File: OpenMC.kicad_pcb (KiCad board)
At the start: 2 copper layers, 38.1 x 38.1 mm, 142 parts, among them J1 Motor Digital, J2 USB-C, J3 CAN, J4 Controller, J5 Motor Analog, SW1 RESET, SW2 BOOT, SW5 POS, U1 ESP32-S3, U3 TCAN332G, U5 NCP163ASN330T1G, Y1 40MHz

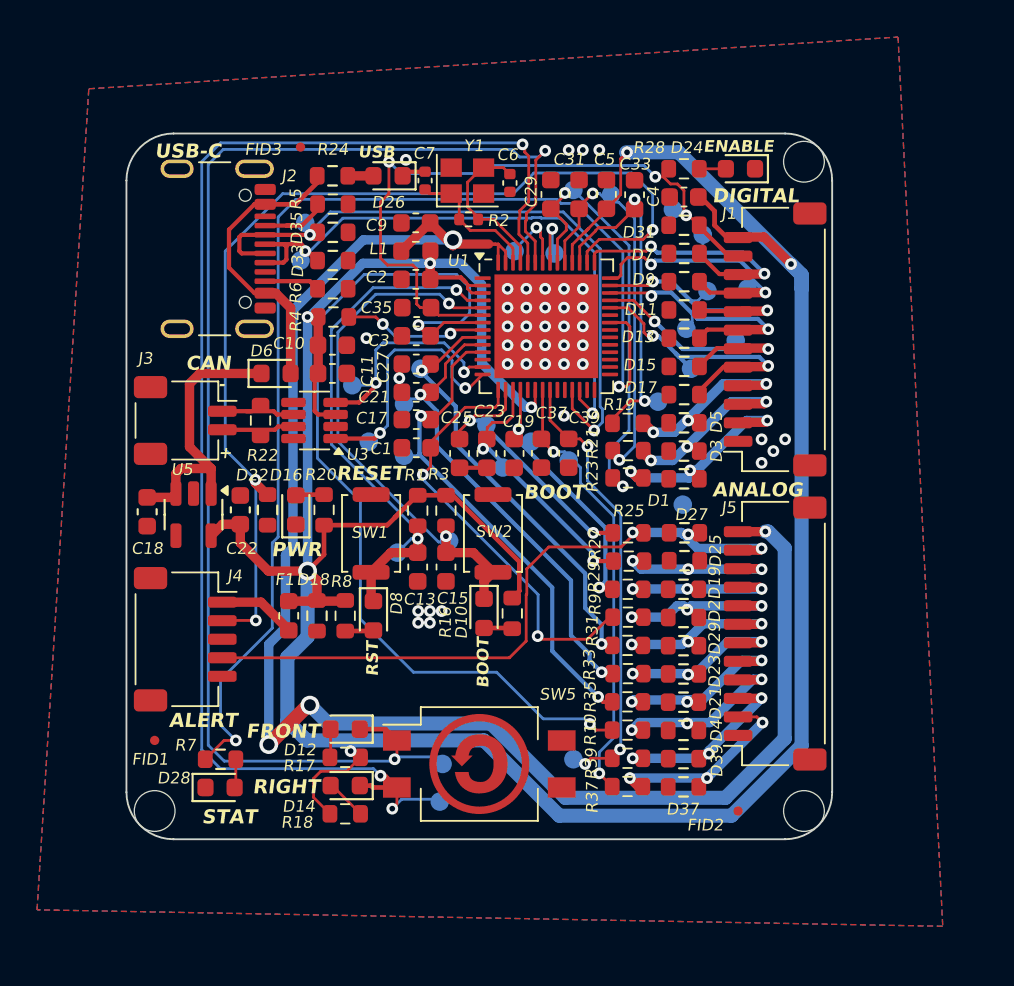
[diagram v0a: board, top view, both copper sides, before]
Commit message: updated to external adc
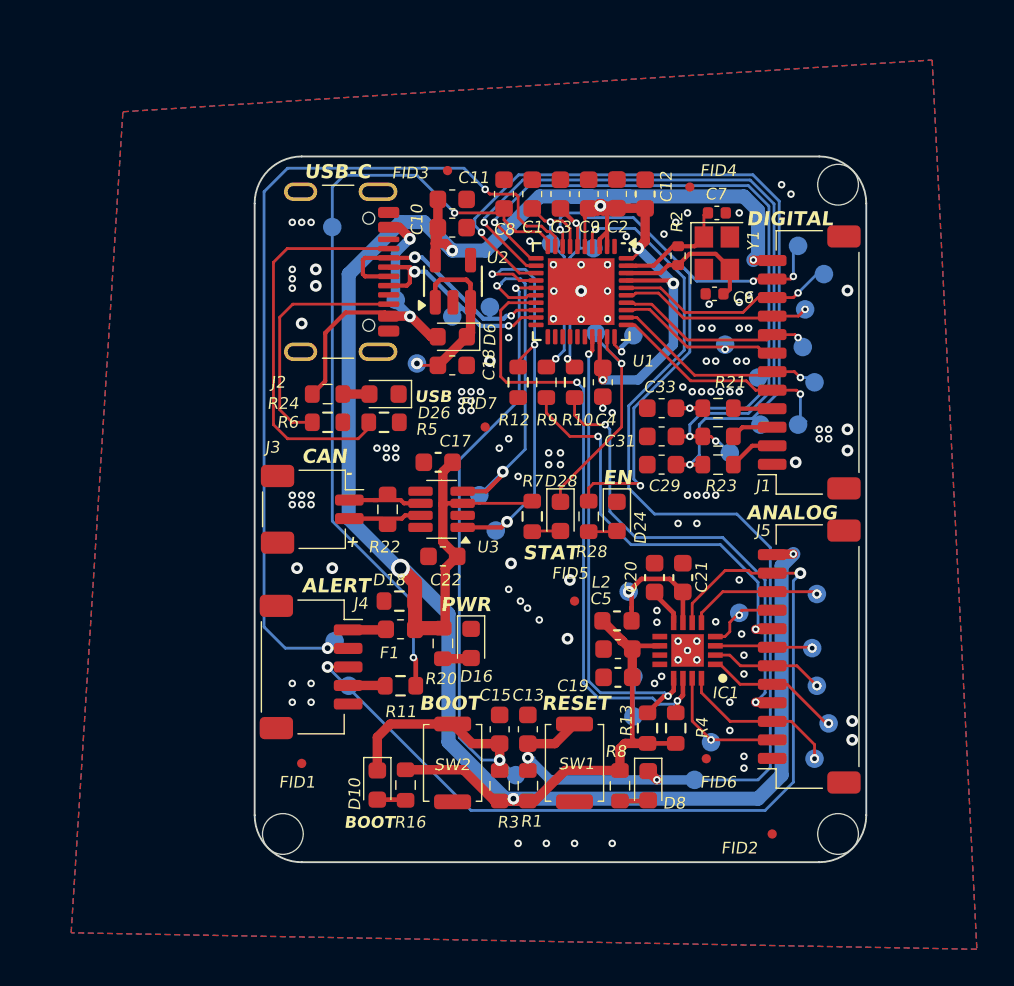
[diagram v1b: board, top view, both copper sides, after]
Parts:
- removed C23, C25, C27, C35, C37, C39: 100nF, Capacitor_SMD:C_0603_1608Metric
- removed D1, D11, D13, D15, D17, D19, D2, D21, D22, D23, D25, D27, D29, D3, D31, D33, D35, D37, D39, D4, D5, D7, D9: 8V, Resistor_SMD:R_0603_1608Metric
- removed D12: Yellow, LED_SMD:LED_0603_1608Metric
- removed D14: Orange, LED_SMD:LED_0603_1608Metric
- removed L1: 100uH, Inductor_SMD:L_0603_1608Metric
- removed R17, R18, R37, R39: 4.7k, Resistor_SMD:R_0603_1608Metric
- removed R25, R27, R29, R31, R33, R35: 10, Resistor_SMD:R_0603_1608Metric
- removed REF**: Symbol_CC-ShareAlike_CopperTop_Small, Symbol:Symbol_CC-ShareAlike_CopperTop_Small
- removed REF**: OSHW-Logo2_7.3x6mm_SilkScreen, Symbol:OSHW-Logo2_7.3x6mm_SilkScreen
- removed REF**: ESD-Logo_6.6x6mm_SilkScreen, Symbol:ESD-Logo_6.6x6mm_SilkScreen
- removed REF**: Symbol_CreativeCommons_SilkScreenTop_Type2_Big, Symbol:Symbol_CreativeCommons_SilkScreenTop_Type2_Big
- removed REF**: WEEE-Logo_4.2x6mm_SilkScreen, Symbol:WEEE-Logo_4.2x6mm_SilkScreen
- removed SW5: POS, Button_Switch_SMD:SW_DIP_SPSTx02_Slide_Omron_A6S-210x_W8.9mm_P2.54mm
- removed U5: NCP163ASN330T1G, Package_TO_SOT_SMD:SOT-23-5
- added C12: 4.7uF, Capacitor_SMD:C_0603_1608Metric, F.Cu at (113.8, 46.2)
- added C20: 1uF, Capacitor_SMD:C_0603_1608Metric, F.Cu at (114.3, 66.9)
- added C8: 4.7uF, Capacitor_SMD:C_0603_1608Metric, F.Cu at (106.2, 46.2)
- added FID4: Fiducial, Fiducial:Fiducial_0.5mm_Mask1mm, F.Cu at (116.2, 45.8)
- added FID5: Fiducial, Fiducial:Fiducial_0.5mm_Mask1mm, F.Cu at (110.0, 68.2)
- added FID6: Fiducial, Fiducial:Fiducial_0.5mm_Mask1mm, F.Cu at (117.1, 76.7)
- added FID7: Fiducial, Fiducial:Fiducial_0.5mm_Mask1mm, F.Cu at (105.2, 58.8)
- added IC1: TLA2528IRTER, OpenMC:QFN50P300X300X80-17N-D, F.Cu at (116.1, 70.9)
- added L2: 1uH, Inductor_SMD:L_0603_1608Metric, F.Cu at (112.3, 69.3)
- added R11: 4.7k, Resistor_SMD:R_0603_1608Metric, F.Cu at (100.6, 72.8)
- added R12: 4.7k, Resistor_SMD:R_0603_1608Metric, F.Cu at (106.9, 56.4)
- added R13: 2.2k, Resistor_SMD:R_0603_1608Metric, F.Cu at (113.9, 75.1)
- added SYM1: Logo_Open_Hardware_Small, Symbol:OSHW-Symbol_6.7x6mm_SilkScreen, B.Cu at (116.7, 49.1)
- added TP30: V_SENSE.B, TestPoint:TestPoint_Pad_D1.0mm, B.Cu at (123.1, 67.8)
- added TP31: V_SENSE.A, TestPoint:TestPoint_Pad_D1.0mm, B.Cu at (97.8, 72.8)
- added TP32: V_{A}, TestPoint:TestPoint_Pad_D1.0mm, B.Cu at (112.9, 67.7)
- added TP33: V_GAIN_SENSE, TestPoint:TestPoint_Pad_D1.0mm, B.Cu at (117.3, 75.8)
- added TP34: I_GAIN_SENSE, TestPoint:TestPoint_Pad_D1.0mm, B.Cu at (122.9, 76.7)
- added TP35: ~{INT}, TestPoint:TestPoint_Pad_D1.0mm, B.Cu at (97.0, 70.4)
- added U2: AP2204K-3.3, Package_TO_SOT_SMD:SOT-23-5, F.Cu at (103.4, 50.9)
- C17, C21: value 100nF -> 4.7uF
- D18: value 8V -> 10V; footprint Resistor_SMD:R_0603_1608Metric -> OpenMC:R_0603_1608Metric
- D26: value BLUE -> Blue
- D6: value 600mV -> 430mV
- R4: value 10k -> 2.2k
- TP1: value IGAIN_SENSE -> MOT_TEMP_SENSE
- TP13: value BACK -> SDA
- TP14: value LEFT -> SCL
- TP15: value VA_SENSE -> Net-(D6-K)
- TP16: value VB_SENSE -> V_{IN}
- TP17: value VC_SENSE -> I_SENSE.C
- TP18: value IC_SENSE -> I_SENSE.B
- TP19: value IB_SENSE -> I_SENSE.A
- TP20: value IA_SENSE -> V_SENSE.C
- TP7: value GND -> DRV_TEMP_SENSE
- TP8: value VGAIN_SENSE -> SPEED_SENSE
- U1: value ESP32-S3 -> ESP32-C6; footprint Package_DFN_QFN:QFN-56-1EP_7x7mm_P0.4mm_EP5.6x5.6mm -> Package_DFN_QFN:QFN-40-1EP_5x5mm_P0.4mm_EP3.6x3.6mm
- U3: value TCAN332G -> TCAN334
- Y1: value 40MHz -> 40MHz
- moved R4 28.9 mm to (115.4, 75.1), turned to -90 degrees
- moved TP1 27.6 mm to (111.0, 49.1)
- moved TP19 25.7 mm to (122.8, 70.7)
- moved TP18 25.5 mm to (123.1, 72.8)
- moved C5 24.6 mm to (112.3, 70.8), turned to 180 degrees
- moved D28 23.5 mm to (109.2, 63.6), turned to -90 degrees
- moved TP17 22.1 mm to (123.7, 74.8)
- moved TP20 21.7 mm to (118.9, 68.8)
- moved R7 21.3 mm to (107.7, 63.6), turned to 90 degrees
- moved TP25 20.2 mm to (116.5, 77.9), turned to 0 degrees
- moved D24 19.9 mm to (112.3, 63.6), turned to -90 degrees
- moved R28 19.5 mm to (110.7, 63.6), turned to -90 degrees
- moved R10 19.0 mm to (110.0, 56.4), turned to -90 degrees
- moved C18 18.3 mm to (103.4, 55.5), turned to 0 degrees
- moved TP8 17.9 mm to (96.9, 48.0)
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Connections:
- net /CAN Transciever/TX renamed /TX
- C1 pad 1: /Motor Controller /DRV_TEMP -> /Motor Controller /DRV_TEMP_SENSE
- C10 pad 1: VDD3P3 -> /Motor Controller /V_{DD}
- C11 pad 1: VDD3P3 -> /Motor Controller /V_{DD}
- C17 pad 1: /Motor Controller /IC_SENSE -> /Motor Controller /V_{DD}
- C19 pad 1: /Motor Controller /VC_SENSE -> /Motor Controller /V_{DD}
- C2 pad 1: VDD3P3 -> /Motor Controller /V_{DD}
- C21 pad 1: /Motor Controller /IB_SENSE -> /ADC/V_{A}
- C22 pad 1: VDD3P3 -> /Motor Controller /V_{DD}
- C3 pad 1: /Motor Controller /MOT_TEMP -> /Motor Controller /MOT_TEMP_SENSE
- C4 pad 1: VDD3P3 -> /Motor Controller /V_{DD}
- C5 pad 1: VDD3P3 -> /Motor Controller /V_{DD}
- C9 pad 1: /V_{ANA} -> /Motor Controller /V_{DD}
- D18 pad 2: VDD3P3 -> /Motor Controller /V_{DD}
- D28 pad 1: /GND -> /Motor Controller /TXD
- D6 pad 2: /VBUS -> /V_{BUS}
- F1 pad 1: VDD3P3 -> /Motor Controller /V_{DD}
- J1 pad 12: VDD3P3 -> /Motor Controller /V_{DD}
- J1 pad MP: (no net) -> /GND
- J2 pad A4: /VBUS -> /V_{BUS}
- J2 pad A9: /VBUS -> /V_{BUS}
- J2 pad B4: /VBUS -> /V_{BUS}
- J2 pad B9: /VBUS -> /V_{BUS}
- J3 pad MP: (no net) -> /GND
- J4 pad 3: /GND -> /V_SENSE.A
- J4 pad 4: /V_SENSE.A -> /SPEED_CTRL_SENSE
- J4 pad MP: (no net) -> /GND
- J5 pad 12: /V_{ANA} -> /Motor Controller /V_{DD}
- J5 pad MP: (no net) -> /GND
- R1 pad 2: VDD3P3 -> /Motor Controller /V_{DD}
- R10 pad 1: /Motor Controller /MOT_TEMP -> /Motor Controller /MOT_TEMP_SENSE
- R16 pad 2: VDD3P3 -> /Motor Controller /V_{DD}
- R20 pad 1: VDD3P3 -> /Motor Controller /V_{DD}
- R24 pad 1: /VBUS -> /V_{BUS}
- R3 pad 2: VDD3P3 -> /Motor Controller /V_{DD}
- R4 pad 1: Net-(U1-GPIO3/ADC1_CH2) -> /SDA
- R4 pad 2: VDD3P3 -> /Motor Controller /V_{DD}
- R7 pad 2: /Motor Controller /STAT -> /Motor Controller /V_{DD}
- R8 pad 2: VDD3P3 -> /Motor Controller /V_{DD}
- R9 pad 1: /Motor Controller /DRV_TEMP -> /Motor Controller /DRV_TEMP_SENSE
- TP1 pad 1: /Motor Controller /IGAIN_SENSE -> /Motor Controller /MOT_TEMP_SENSE
- TP13 pad 1: /Motor Controller /BACK -> /SDA
- TP14 pad 1: /Motor Controller /LEFT -> /SCL
- TP15 pad 1: /Motor Controller /VA_SENSE -> Net-(D6-K)
- TP16 pad 1: /Motor Controller /VB_SENSE -> /V_{BUS}
- TP17 pad 1: /Motor Controller /VC_SENSE -> /I_SENSE.C
- TP18 pad 1: /Motor Controller /IC_SENSE -> /I_SENSE.B
- TP19 pad 1: /Motor Controller /IB_SENSE -> /I_SENSE.A
- TP20 pad 1: /Motor Controller /IA_SENSE -> /V_SENSE.C
- TP28 pad 1: /CAN Transciever/RX -> /RX
- TP7 pad 1: /GND -> /Motor Controller /DRV_TEMP_SENSE
- TP8 pad 1: /Motor Controller /VGAIN_SENSE -> /Motor Controller /SPEED_SENSE
- U1 pad 1: unconnected-(U1-LNA_IN/RF-Pad1) -> Net-(U1-ANT)
- U1 pad 10: /Motor Controller /IB_SENSE -> /Motor Controller /SPEED_SENSE
- U1 pad 11: /Motor Controller /IC_SENSE -> /Motor Controller /HALL_A
- U1 pad 12: unconnected-(U1-GPIO7/ADC1_CH6-Pad12) -> /Motor Controller /HALL_B
- U1 pad 13: /CAN Transciever/RX -> /Motor Controller /HALL_C
- U1 pad 15: /Motor Controller /DRV_TEMP -> /Motor Controller /BOOT
- U1 pad 16: /Motor Controller /VA_SENSE -> /RX
- U1 pad 17: /Motor Controller /VB_SENSE -> /SDA
- U1 pad 18: /Motor Controller /VC_SENSE -> /D-
- U1 pad 19: unconnected-(U1-GPIO14/ADC2_CH3-Pad19) -> /D+
- U1 pad 2: VDD3P3 -> /Motor Controller /V_{DD}
- U1 pad 20: VDD3P3 -> unconnected-(U1-SPICS0/GPIO24-Pad20)
- U1 pad 21: /Motor Controller /VGAIN_SENSE -> unconnected-(U1-SPIQ/GPIO25-Pad21)
- U1 pad 22: /Motor Controller /IGAIN_SENSE -> unconnected-(U1-SPIWP/GPIO26-Pad22)
- U1 pad 25: /D- -> unconnected-(U1-SPICLK/GPIO29-Pad25)
- U1 pad 26: /D+ -> unconnected-(U1-SPID/GPIO30-Pad26)
- U1 pad 27: unconnected-(U1-GPIO21-Pad27) -> /SCL
- U1 pad 28: unconnected-(U1-SPI_CS1/GPIO26-Pad28) -> /Motor Controller /V_{DD}
- U1 pad 29: unconnected-(U1-VDD_SPI-Pad29) -> /Motor Controller /TXD
- U1 pad 3: VDD3P3 -> /Motor Controller /V_{DD}
- U1 pad 30: unconnected-(U1-SPIHD/GPIO27-Pad30) -> /Motor Controller /RXD
- U1 pad 31: unconnected-(U1-SPIWP/GPIO28-Pad31) -> /CL
- U1 pad 32: unconnected-(U1-SPICS0/GPIO29-Pad32) -> /CH
- U1 pad 33: unconnected-(U1-SPICLK/GPIO30-Pad33) -> /BL
- U1 pad 34: unconnected-(U1-SPIQ/GPIO31-Pad34) -> /BH
- U1 pad 35: unconnected-(U1-SPID/GPIO32-Pad35) -> /AL
- U1 pad 36: /Motor Controller /STAT -> /AH
- U1 pad 37: unconnected-(U1-SPICLK_P/GPIO47-Pad37) -> /Motor Controller /V_{DD}
- U1 pad 38: /CL -> /Motor Controller /X-
- U1 pad 39: /CH -> /Motor Controller /X+
- U1 pad 40: /BL -> /Motor Controller /V_{DD}
- U1 pad 41: /BH -> /GND
- U1 pad 5: /Motor Controller /BOOT -> /Motor Controller /V_{DD}
- U1 pad 6: /DRV_EN -> /Motor Controller /MOT_TEMP_SENSE
- U1 pad 7: /Motor Controller /MOT_TEMP -> /Motor Controller /DRV_TEMP_SENSE
- U1 pad 8: Net-(U1-GPIO3/ADC1_CH2) -> /DRV_EN
- U1 pad 9: /Motor Controller /IA_SENSE -> /~{INT}
- U3 pad 3: VDD3P3 -> /Motor Controller /V_{DD}
- U3 pad 4: /CAN Transciever/RX -> /RX
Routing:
- net VDD3P3: track 179.8 -> 0.00 mm, vias 7 -> 0
- net /Motor Controller /V_{DD}: track 0.00 -> 172.7 mm, vias 0 -> 9
- net /V_{ANA}: track 88.3 -> 0.00 mm, vias 4 -> 0
- net /Motor Controller /LEFT: track 74.1 -> 0.00 mm, vias 3 -> 0
- net /Motor Controller /BACK: track 73.3 -> 0.00 mm, vias 2 -> 0
- net /Motor Controller /STAT: track 64.8 -> 0.00 mm, vias 2 -> 0
- net /Motor Controller /MOT_TEMP: track 51.0 -> 0.00 mm, vias 2 -> 0
- net /Motor Controller /SPEED_SENSE: track 0.00 -> 42.4 mm, vias 0 -> 2
- net /SDA: track 0.00 -> 34.8 mm, vias 0 -> 2
- net /Motor Controller /~{RESET}: track 29.9 -> 58.2 mm, vias 2 -> 3
- net /SCL: track 0.00 -> 26.7 mm, vias 0 -> 2
- net /Motor Controller /IC_SENSE: track 26.5 -> 0.00 mm, vias 2 -> 0
- net /D-: track 39.0 -> 13.8 mm
- net /Motor Controller /IB_SENSE: track 25.0 -> 0.00 mm, vias 2 -> 0
- net /Motor Controller /VGAIN_SENSE: track 23.9 -> 0.00 mm, vias 2 -> 0
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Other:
- board size 38.1 x 38.1 mm -> 33 x 38.1 mm
- board text added: "EN"
- board text removed: "ENABLE"
- board text removed: "FRONT"
- board text removed: "RIGHT"
- board text removed: "RST"

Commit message: hello
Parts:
- removed FID4, FID5, FID6, FID7: Fiducial, Fiducial:Fiducial_0.5mm_Mask1mm
- TP15: value Net-(D6-K) -> VIN
- TP21: value DRIVER_ENABLE -> DVR_EN
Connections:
- net Net-(D6-K) renamed /3 Volt Supply/VIN
